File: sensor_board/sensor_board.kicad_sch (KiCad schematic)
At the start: 45 parts, among them J1 zigbee connector, J2 SWD, J3 110990030, J4 AM2320, J5 Lithium_battery_conn, Q1 SI2300DS, Q2 SI2301DS, U1 MCP6002-xMC, U2 MIC5365-3.3YC5, U3 STM32L051C8Tx

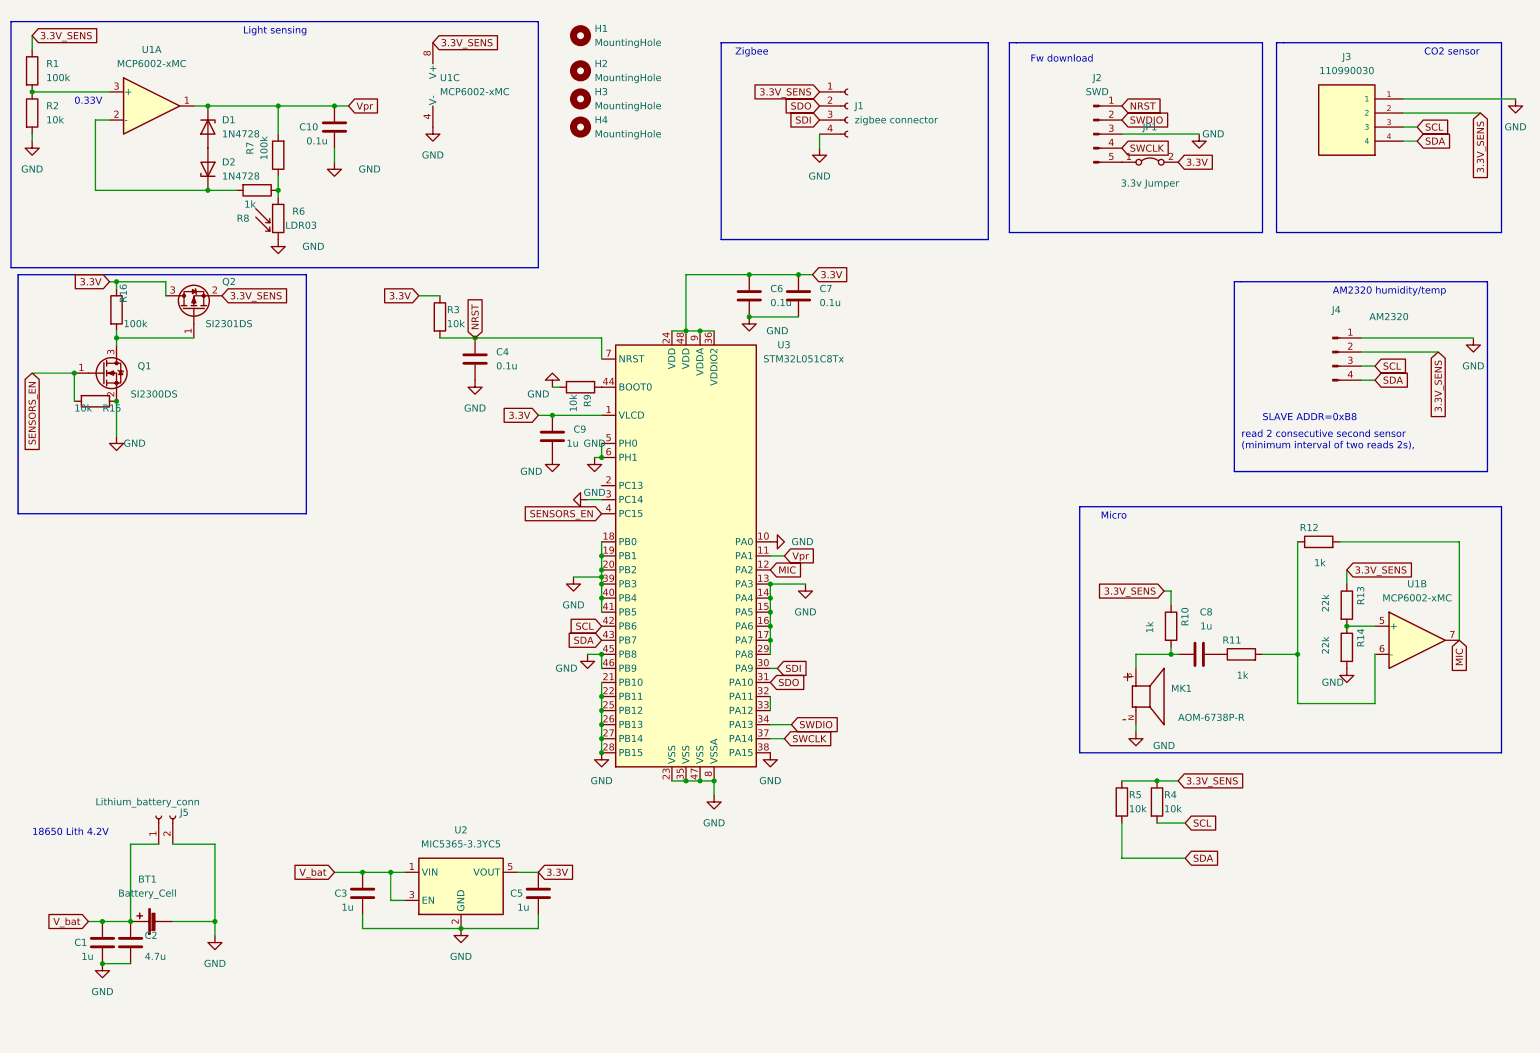
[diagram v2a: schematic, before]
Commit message: 1. modify schematic, replace mosfet which control sensors power with LDO IC 2. add accelerator sensor to measure wind speed 3. ..
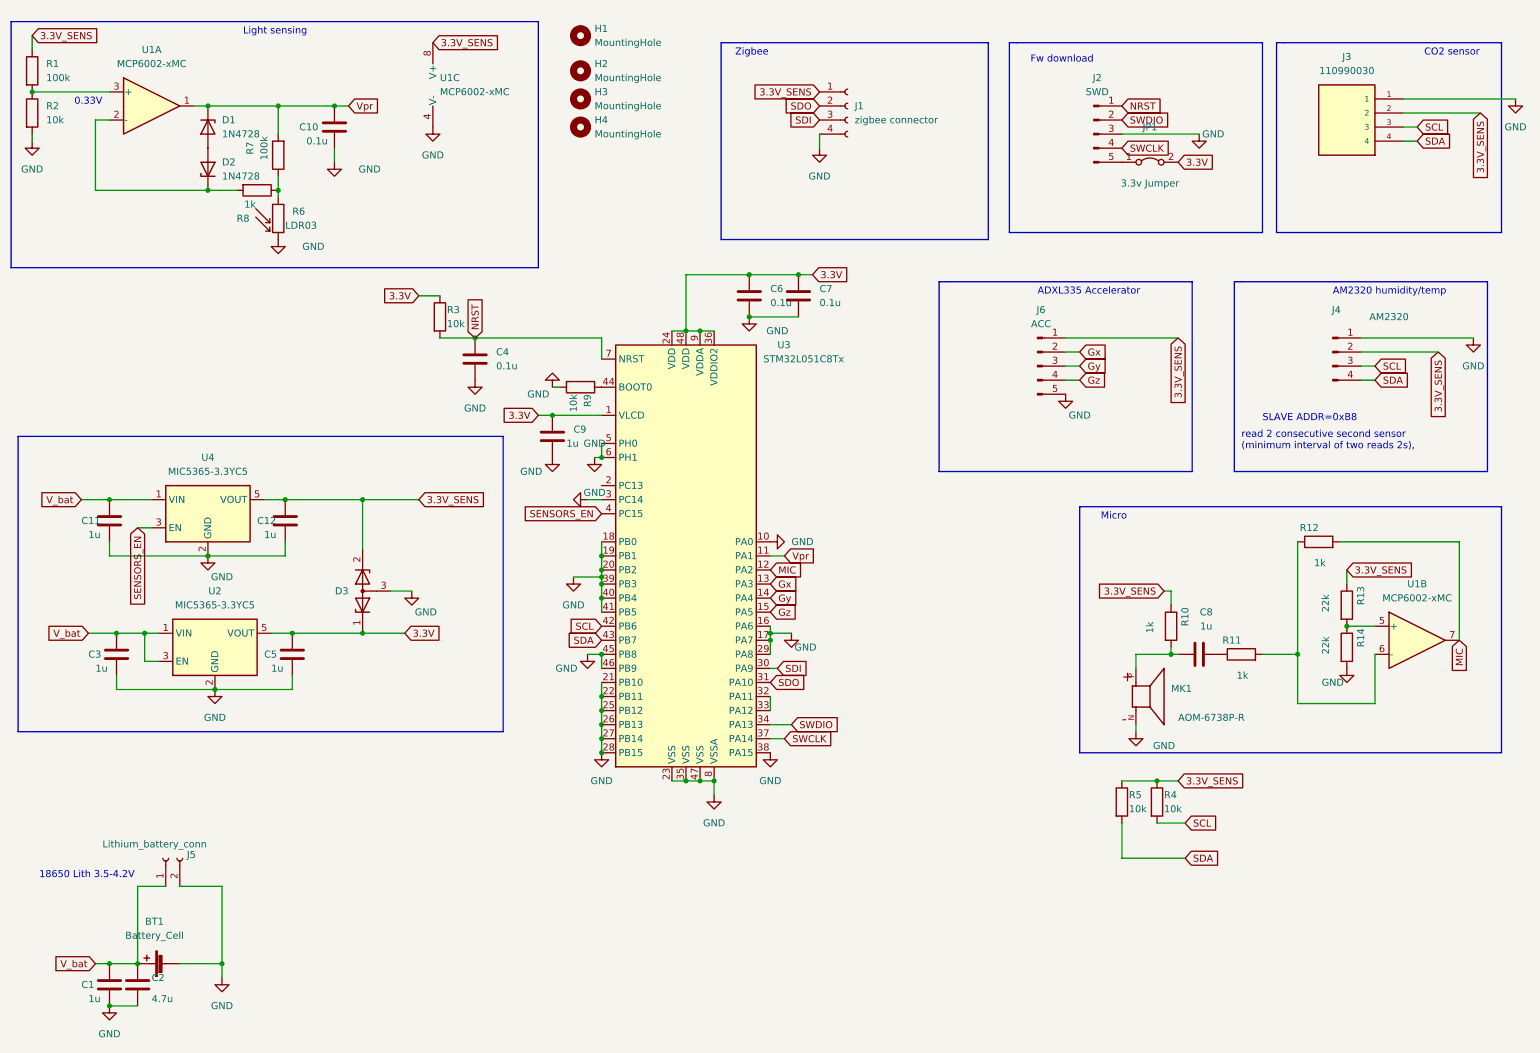
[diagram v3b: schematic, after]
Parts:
- removed Q1: SI2300DS, Package_TO_SOT_SMD:SOT-23_Handsoldering, symbol Device:Q_NMOS_GSD
- removed Q2: SI2301DS, Package_TO_SOT_SMD:SOT-23, symbol Device:Q_PMOS_GSD
- removed R15: 10k, Resistor_SMD:R_0805_2012Metric_Pad1.20x1.40mm_HandSolder, symbol Device:R
- removed R16: 100k, Resistor_SMD:R_0805_2012Metric_Pad1.20x1.40mm_HandSolder, symbol Device:R
- added C11, C12: 1u, Capacitor_SMD:C_1206_3216Metric_Pad1.33x1.80mm_HandSolder, symbol Device:C
- added D3: D_Zener_Dual_CommonAnode_KKA, Package_TO_SOT_SMD:SOT-23, symbol Device:D_Zener_Dual_CommonAnode_KKA
- added J6: ACC, Connector_PinSocket_2.54mm:PinSocket_1x05_P2.54mm_Vertical, symbol Connector:Conn_01x05_Male
- added U4: MIC5365-3.3YC5, Package_TO_SOT_SMD:SOT-353_SC-70-5, symbol Regulator_Linear:MIC5365-3.3YC5
- J1: footprint Connector_PinSocket_1.27mm:PinSocket_1x04_P1.27mm_Vertical -> Connector_PinSocket_2.54mm:PinSocket_1x04_P2.54mm_Vertical
- J2: footprint Connector_PinHeader_1.27mm:PinHeader_1x05_P1.27mm_Vertical -> Connector_PinSocket_2.54mm:PinSocket_1x05_P2.54mm_Vertical
- J4: footprint Connector:NS-Tech_Grove_1x04_P2mm_Vertical -> Connector_PinSocket_2.54mm:PinSocket_1x04_P2.54mm_Vertical
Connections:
- net 3.3V: now also D3.1 (K)
- net 3.3V_SENS: now also C12.1, D3.2 (K), J6.1 (Pin_1), U4.5 (VOUT)
- net GND: now also C11.2, C12.2, D3.3 (A), J6.5 (Pin_5), U4.2 (GND); no longer U3.13 (PA3), U3.14 (PA4), U3.15 (PA5)
- net SENSORS_EN: now also U4.3 (EN)
- net V_bat: now also C11.1, U4.1 (VIN)
- new net Gx: J6.2 (Pin_2), U3.13 (PA3)
- new net Gy: J6.3 (Pin_3), U3.14 (PA4)
- new net Gz: J6.4 (Pin_4), U3.15 (PA5)
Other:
- note added: "18650 Lith 3.5-4.2V"
- note added: "ADXL335 Accelerator"
- note removed: "18650 Lith 4.2V"
- moved on the sheet: BT1, C1, C2, C3, C5, J5, U2

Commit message: 1. use sensorion scd42 for lower power 2. add usb micro B for testing or using with backup battery later 3. add signal RC filter
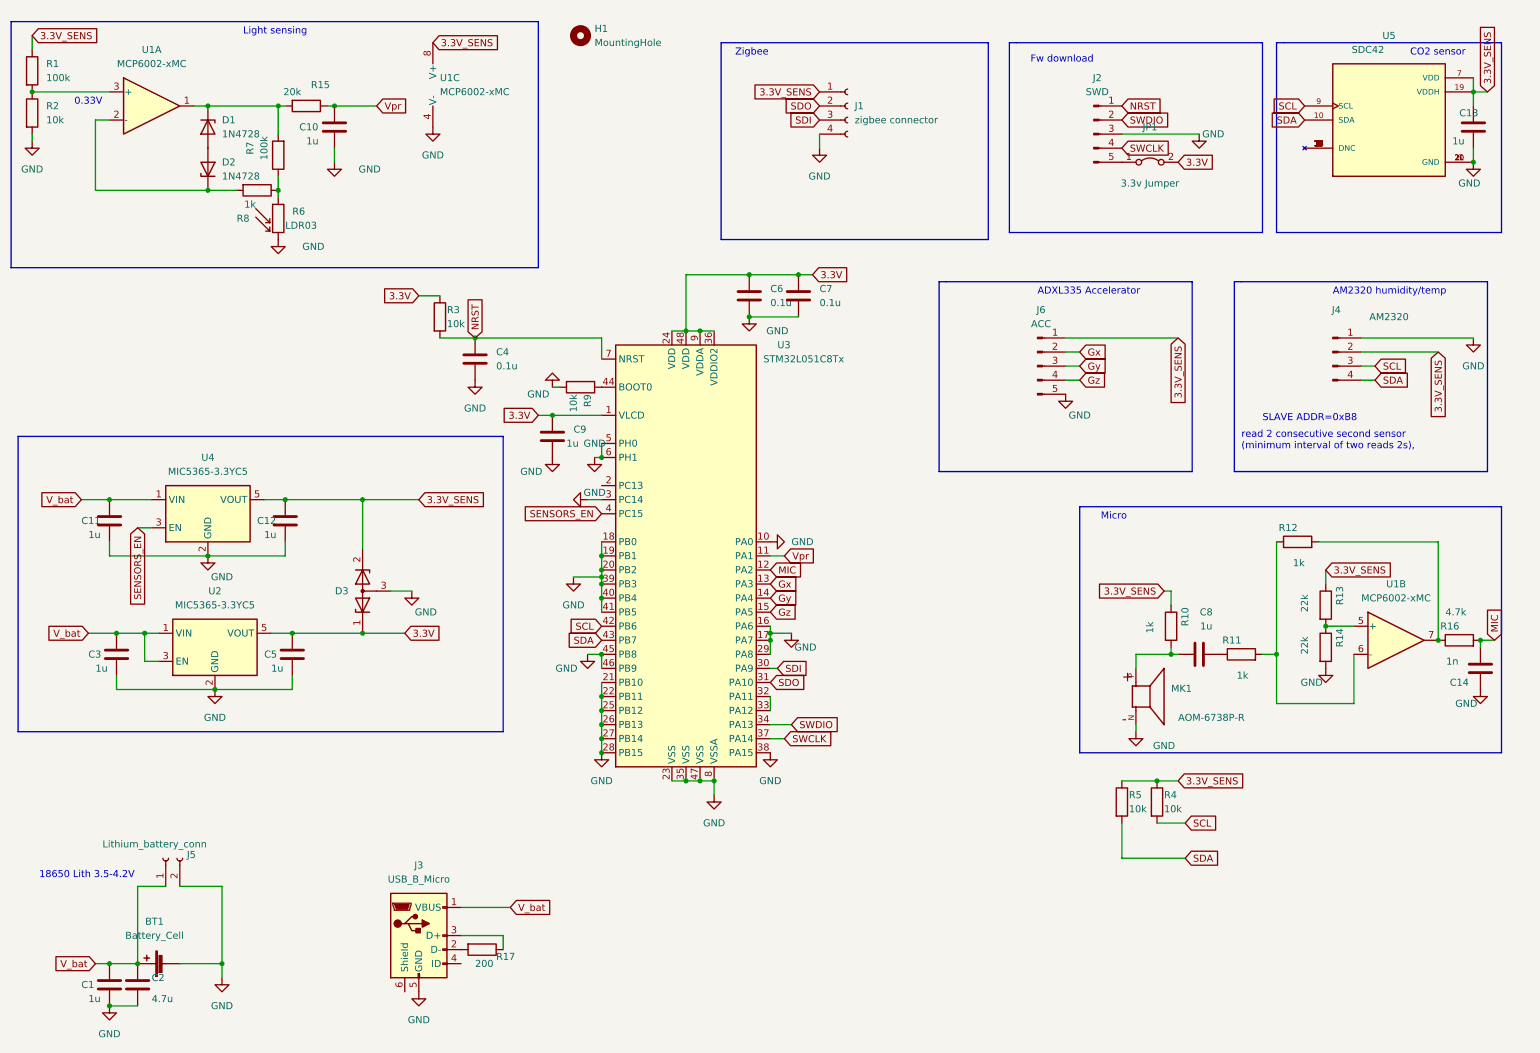
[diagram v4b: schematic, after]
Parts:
- removed H2, H3, H4: MountingHole, MountingHole:MountingHole_2.7mm_M2.5_Pad, symbol Mechanical:MountingHole
- removed J3: 110990030, SEEED_110990030, symbol 1x04 grove:110990030
- added C13: 1u, Capacitor_SMD:C_1206_3216Metric_Pad1.33x1.80mm_HandSolder, symbol Device:C
- added C14: 1n, Capacitor_SMD:C_1206_3216Metric_Pad1.33x1.80mm_HandSolder, symbol Device:C
- added J3: USB_B_Micro, Connector_USB:USB_Micro-B_Wuerth_629105150521, symbol Connector:USB_B_Micro
- added R15: 20k, Resistor_SMD:R_0805_2012Metric_Pad1.20x1.40mm_HandSolder, symbol Device:R
- added R16: 4.7k, Resistor_SMD:R_0805_2012Metric_Pad1.20x1.40mm_HandSolder, symbol Device:R
- added R17: 200, Resistor_SMD:R_0805_2012Metric_Pad1.20x1.40mm_HandSolder, symbol Device:R
- added U5: SDC42, SCD41-D-R2:XDCR_SCD41-D-R2, symbol SCD41-D-R2:SCD41-D-R2
- C10: value 0.1u -> 1u
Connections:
- net 3.3V_SENS: now also C13.1, U5.19 (VDDH), U5.7 (VDD)
- net GND: now also C13.2, C14.1, J3.5 (GND), U5.20 (GND), U5.21 (GND), U5.6 (GND)
- net MIC: now also C14.2, R16.2; no longer R12.2, U1.7
- net SCL: now also U5.9 (SCL)
- net SDA: now also U5.10 (SDA)
- net V_bat: now also J3.1 (VBUS)
- net Vpr: now also R15.1; no longer D1.1 (K), R7.2, U1.1
- new net: R12.2, R16.1, U1.7
- new net: D1.1 (K), R15.2, R7.2, U1.1
- new net: U5.1 (DNC), U5.11 (DNC), U5.12 (DNC), U5.13 (DNC), U5.14 (DNC), U5.15 (DNC), U5.16 (DNC), U5.17 (DNC), U5.18 (DNC), U5.2 (DNC), U5.3 (DNC), U5.4 (DNC), U5.5 (DNC), U5.8 (DNC)
- new net: J3.2 (D-), R17.2
- new net: J3.3 (D+), R17.1
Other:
- moved on the sheet: R12, R13, R14, U1B

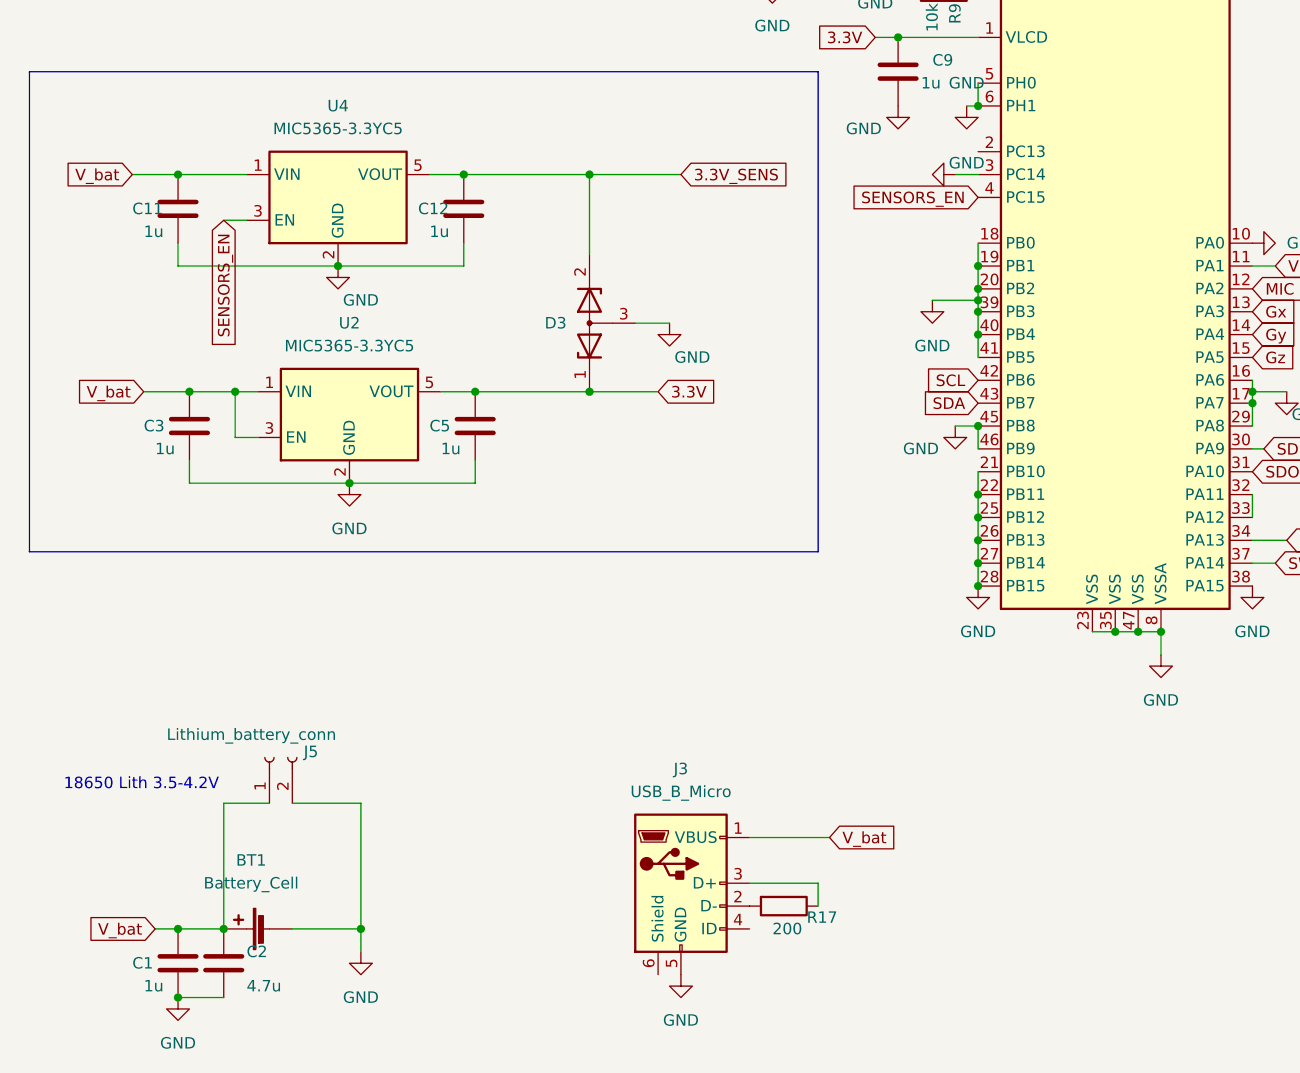
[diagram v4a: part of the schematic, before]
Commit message: add reverse polarity protection mosfet and diode
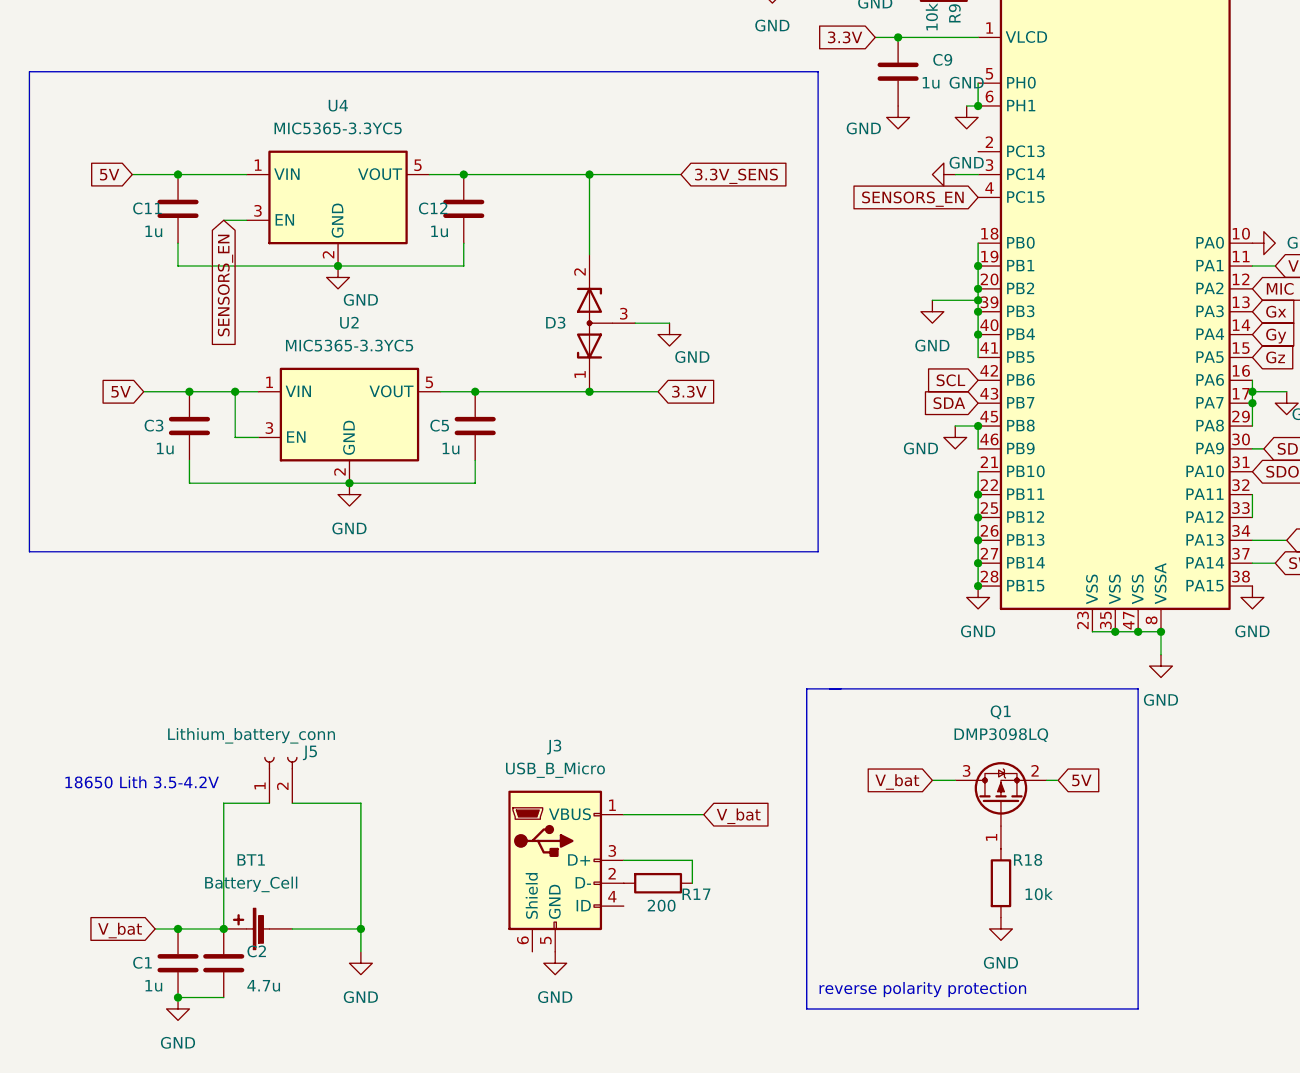
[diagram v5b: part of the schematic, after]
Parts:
- added Q1: DMP3098LQ, Package_TO_SOT_SMD:SOT-23, symbol Device:Q_PMOS_GSD
- added R18: 10k, Resistor_SMD:R_0805_2012Metric_Pad1.20x1.40mm_HandSolder, symbol Device:R
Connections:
- net GND: now also R18.2
- net V_bat: now also Q1.3 (D); no longer C11.1, C3.1, U2.1 (VIN), U2.3 (EN), U4.1 (VIN)
- new net: Q1.1 (G), R18.1
- new net 5V: C11.1, C3.1, Q1.2 (S), U2.1 (VIN), U2.3 (EN), U4.1 (VIN)
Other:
- note added: "reverse polarity protection"
- moved on the sheet: J3, R17
